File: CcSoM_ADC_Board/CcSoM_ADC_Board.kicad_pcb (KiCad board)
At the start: 4 copper layers, 160 x 100 mm, 159 parts, among them J1 SoM Connector, J12 USB_C_Receptacle_USB2.0_16P, J13 Conn_02x03_Odd_Even, J14 Conn_02x03_Odd_Even, J15 Conn_02x02_Counter_Clockwise, J16 Barrel_Jack, J18 USB_A, J19 USB_A, J3 Conn_02x8_Odd_Even, J4 Conn_Coaxial, J5 WE-RJ45_7498111124, J6 Conn_01x14, J7 Conn_01x08, J8 Conn_01x16_Socket, J9 Conn_01x08, SW3 SW_Push, U1 SN74LVC00APWE4, U10 USB3343, U11 RTL8211E-VB-CG, U12 LTC2242IUP-12-PBF, U14 SN74CB3T3306DCTR, U2 74AUP1G04, U3 93LC46B, U4 FT2232HL, U5 SN74CB3T3245PWR, U6 TPS73625DBV, U7 TPS3307-33DR, U8 TPS73633DBV, U9 TXS0202YZPR, X1 12MHz, Y1 25MHz

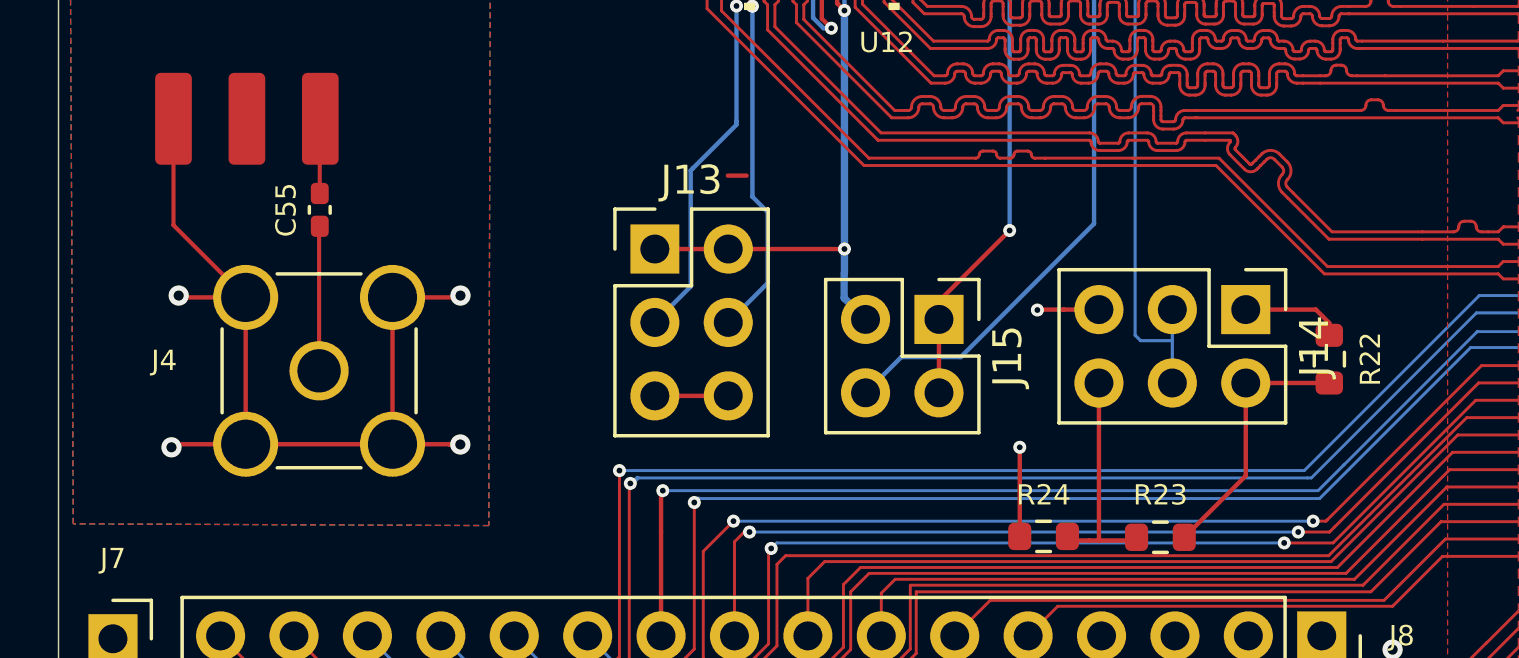
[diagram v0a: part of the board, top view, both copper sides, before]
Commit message: changed digikeyno from component, added info into readme about discontinued parts in digikey
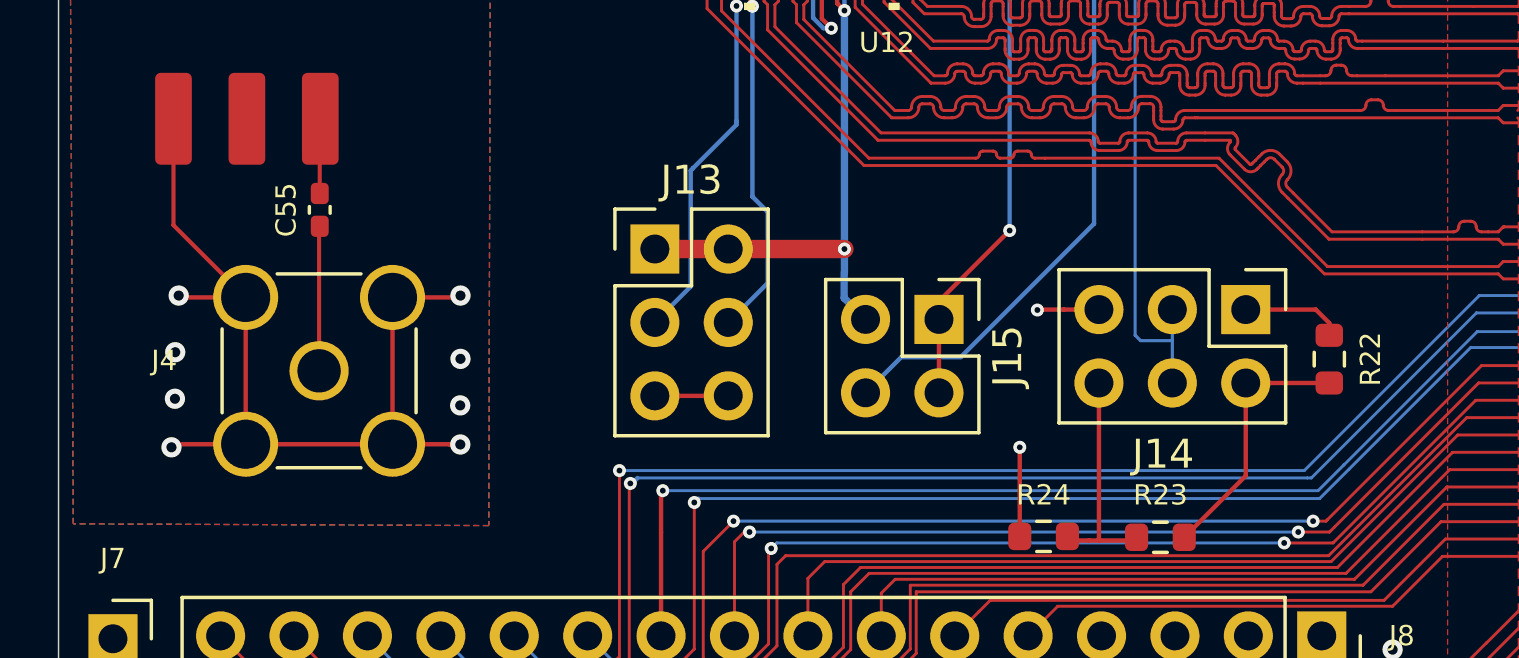
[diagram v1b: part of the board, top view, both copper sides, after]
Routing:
- net OVDD: track 537.4 -> 540.4 mm
- net PRE_BALUN_GND: vias 4 -> 8

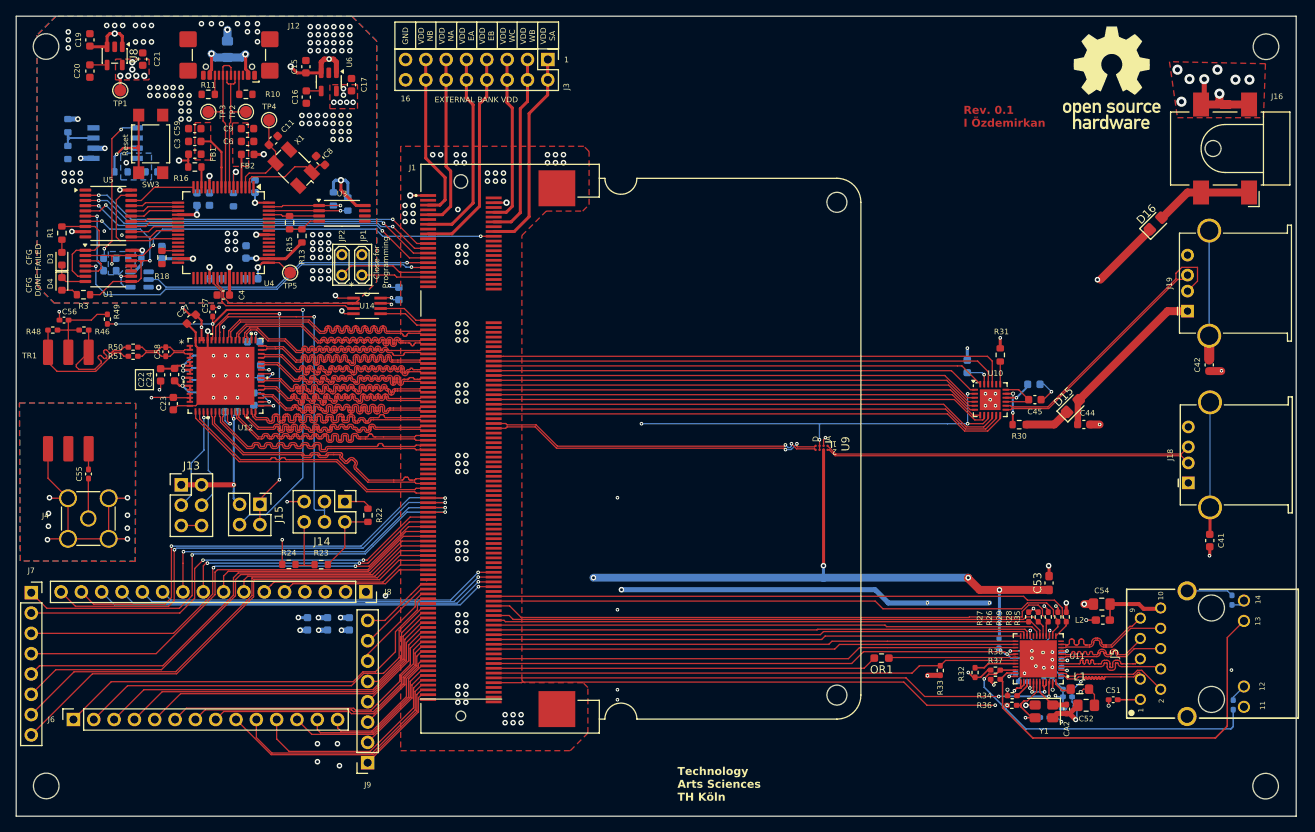
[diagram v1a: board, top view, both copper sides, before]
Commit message: corrected differential pairs
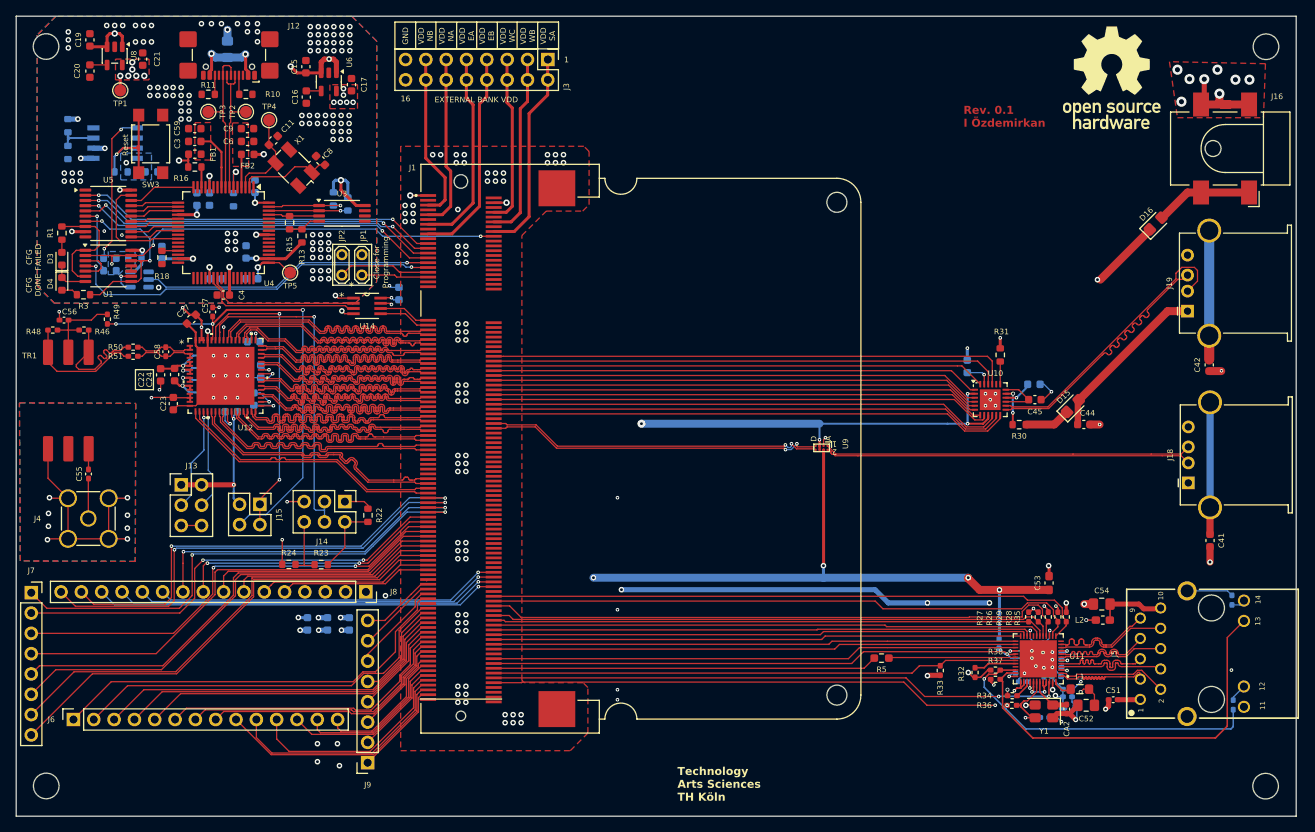
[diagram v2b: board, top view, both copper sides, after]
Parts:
- renumbered OR1 to R5
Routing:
- net USB1_+: track 29.7 -> 34.7 mm
- net OGND: track 121.7 -> 123.1 mm
- net Net-(J5-SGND): track 2.29 -> 2.85 mm

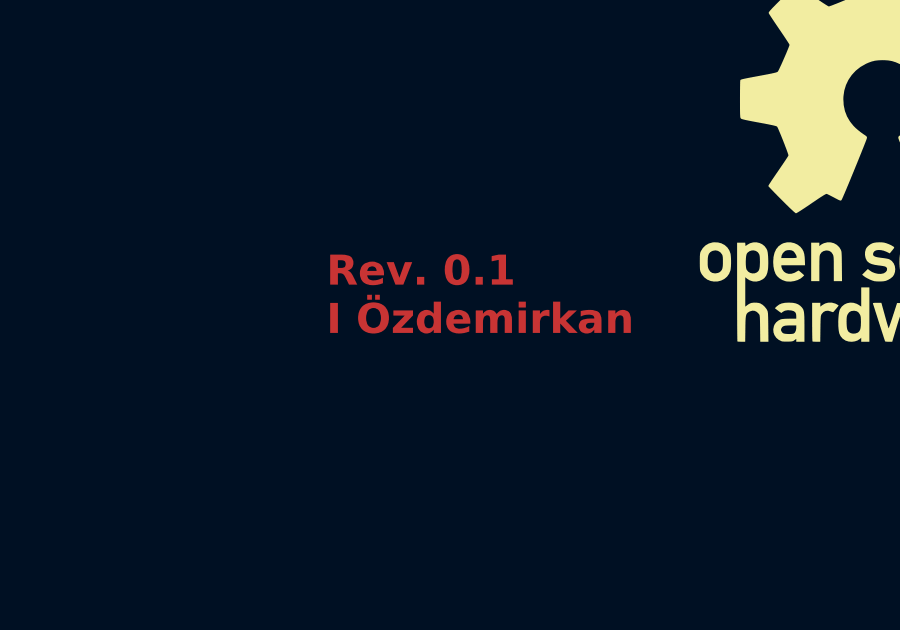
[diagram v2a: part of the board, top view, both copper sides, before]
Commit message: added pcb name on F.Mask
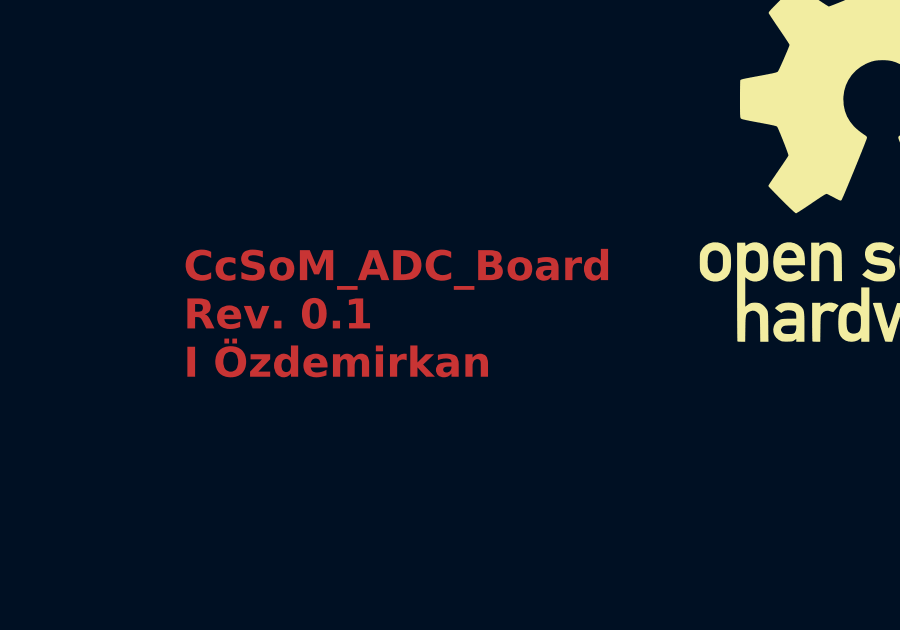
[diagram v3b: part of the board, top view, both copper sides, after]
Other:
- board text added: "CcSoM_ADC_Board Rev. 0.1 I Özdemirkan"
- board text removed: "Rev. 0.1 I Özdemirkan"
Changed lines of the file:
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@@
 		(layer "Edge.Cuts")
 	)
-	(gr_text "Rev. 0.1\nI Özdemirkan"
-		(at 185.5 64.5 0)
+	(gr_text "CcSoM_ADC_Board\nRev. 0.1\nI Özdemirkan"
+		(at 180.74 65.96 0)
 		(layer "F.Cu")
 		(effects
@@
 		)
 	)
+	(gr_text "CcSoM_ADC_Board\nRev. 0.1\nI Özdemirkan"
+		(at 180.73 65.97 0)
+		(layer "F.Mask")
+		(effects
+			(font
+				(size 1 1)
+				(thickness 0.25)
+				(bold yes)
+			)
+			(justify left bottom)
+		)
+	)
 	(gr_text "U11"
 		(at 198.75 131 0)
@@
 		)
 	)
+	(group ""
+		(members "7ba378c7-8571-455a-b2ed-e7ec57e0c6ff" "d592379b-8c39-459f-8403-f0e182f683a4")
+	)
 	(generated
